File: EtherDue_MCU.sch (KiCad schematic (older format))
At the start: 29 parts, among them IC201 ATSAM3X8E, SW201 ERASE, SW202 RESET, U202 FDN340P, U203 LMV358IDGKR, X201 KX-7 12MHz 20pF, X202 32.768kHz

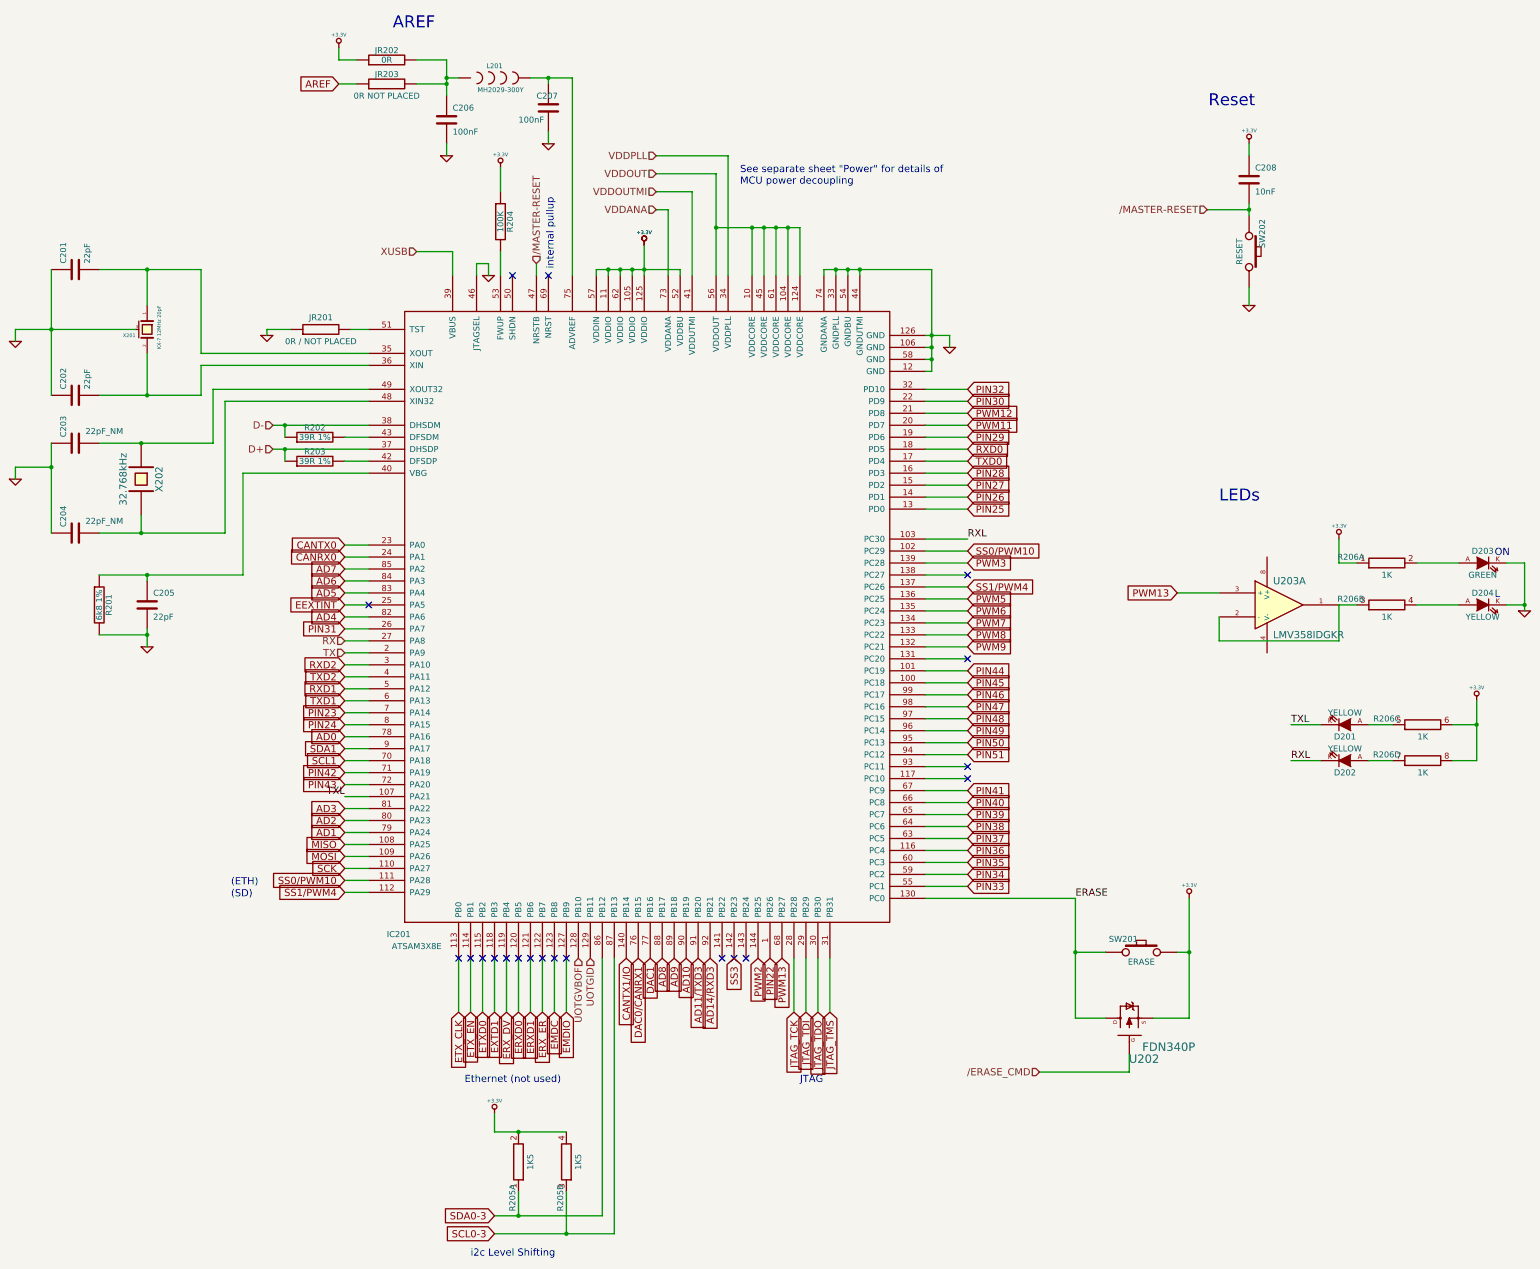
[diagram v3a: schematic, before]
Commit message: Footprints checked, components imported to board but most not placed
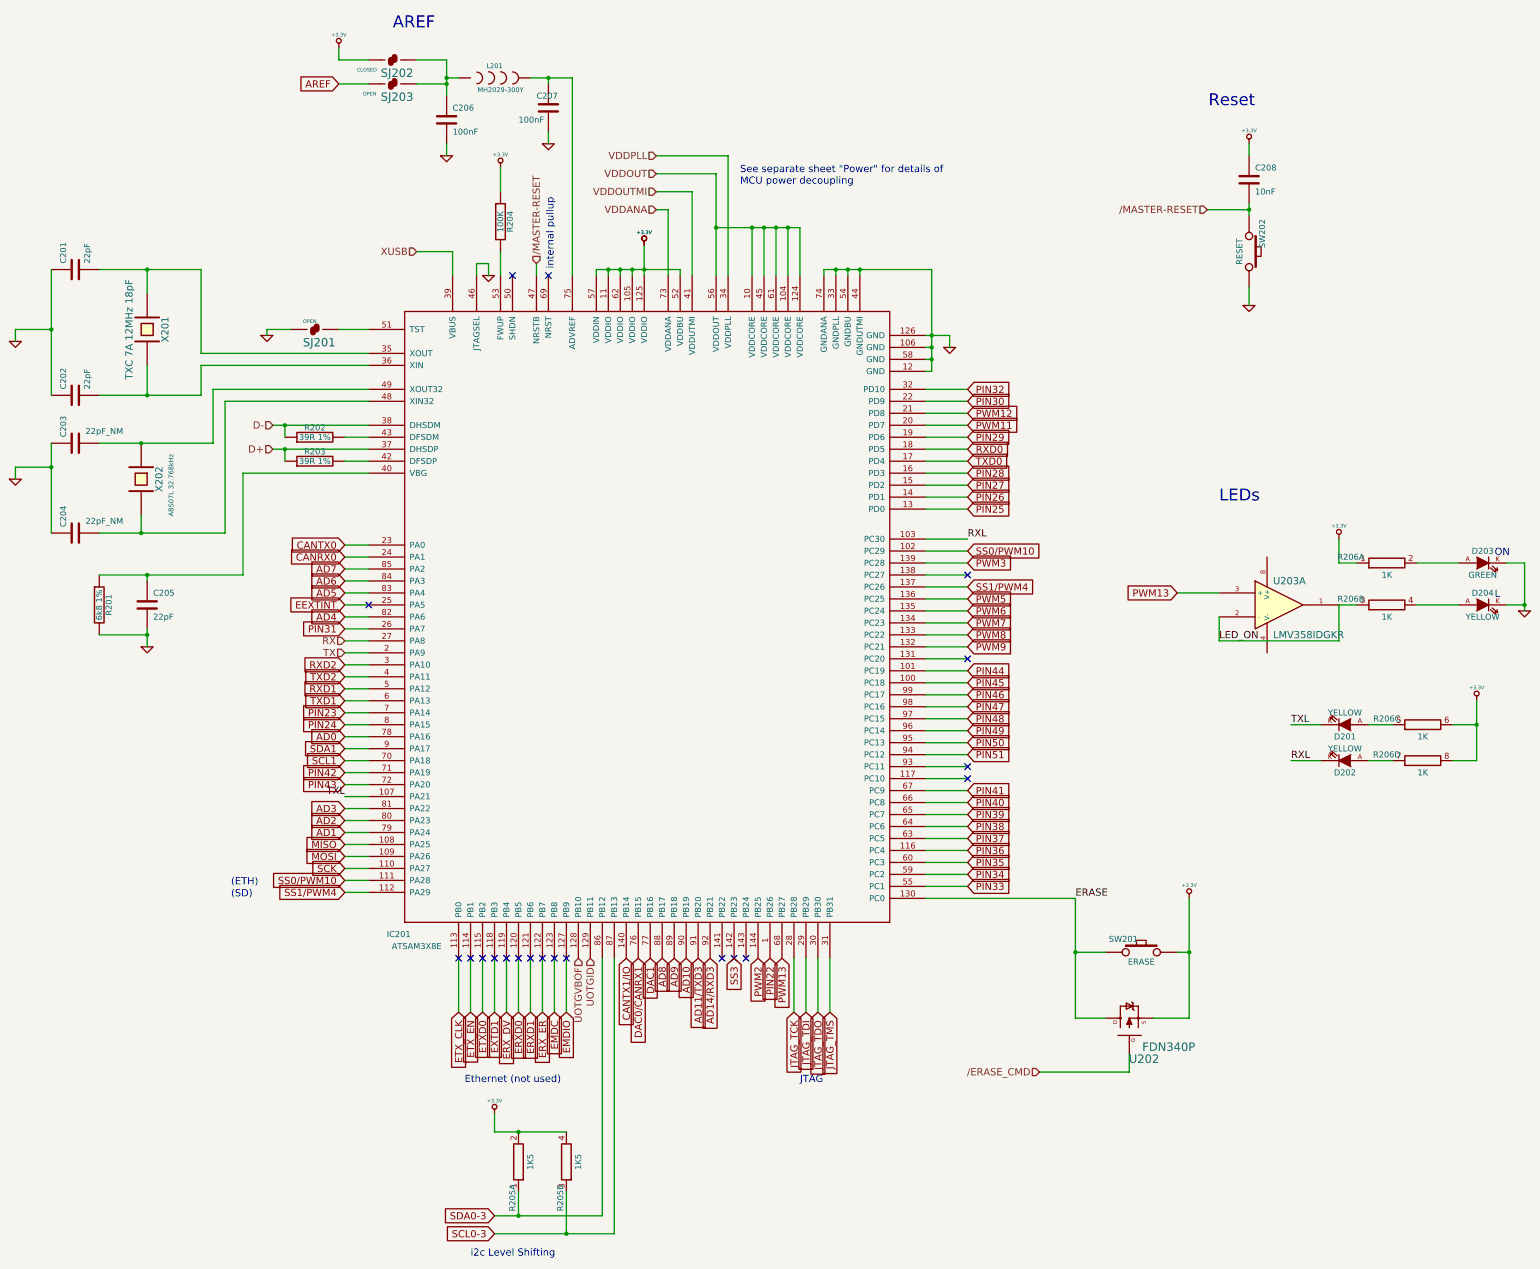
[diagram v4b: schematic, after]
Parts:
- removed JR201: 0R / NOT PLACED, symbol R
- removed JR202: 0R, symbol R
- removed JR203: 0R NOT PLACED, symbol R
- removed X201: KX-7 12MHz 20pF, ~, symbol CRYSTAL_SMD
- added SJ201, SJ203: OPEN, ~, symbol SJ
- added SJ202: CLOSED, ~, symbol SJ
- added X201: TXC 7A 12MHz 18pF, ~, symbol CRYSTAL
- X202: value 32.768kHz -> ABS07L 32.768kHz
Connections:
- net +3.3V: now also SJ202.1
- net AREF: now also SJ203.1
- net GND: now also SJ201.1
- net at C201.2, IC201.35 (XOUT): now also X201.1
- net at C202.2, IC201.36 (XIN): now also X201.2
- net at IC201.51 (TST): now also SJ201.2
- net at C206.1, L201.1: now also SJ202.2, SJ203.2
- net LED_ON: now reaches R206.3 (7), U203.1, U203.2 (-)
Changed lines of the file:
@@
-EESchema Schematic File Version 2  date Tue 04 Jun 2013 15:53:49 EST
+EESchema Schematic File Version 2  date Thu 06 Jun 2013 09:35:07 EST
 LIBS:freetronics_kicad_sch_lib
 LIBS:power
@@
 Sheet 2 6
 Title ""
-Date "4 jun 2013"
+Date "5 jun 2013"
 Rev ""
 Comp ""
@@
 	7700 10750 6700 10750
 Wire Wire Line
-	5400 1150 5550 1150
+	5400 1150 5650 1150
 Connection ~ 6300 1100
 Wire Wire Line
@@
 	4250 2700 4250 3400
 Wire Wire Line
-	5500 3200 5650 3200
+	5400 3200 5650 3200
 Wire Wire Line
 	4800 3250 4800 3200
@@
 	5400 850  5400 950
 Wire Wire Line
-	5400 950  5550 950
+	5400 950  5650 950
 Wire Wire Line
 	7150 1550 7150 1650
@@
 F 3 "" H 6900 10150 60  0001 C CNN
 	1    6900 10150
-	0    -1   -1   0
-$EndComp
-$Comp
-L R JR201
-U 1 1 5163BF82
-P 5250 3200
-F 0 "JR201" V 5350 3200 50  0000 C CNN
-F 1 "0R / NOT PLACED" V 5150 3200 50  0000 C CNN
-F 2 "" H 5250 3200 60  0001 C CNN
-F 3 "" H 5250 3200 60  0001 C CNN
-	1    5250 3200
-	0    -1   -1   0
-$EndComp
-$Comp
-L R JR203
-U 1 1 5163BF2B
-P 5800 1150
-F 0 "JR203" V 5880 1150 50  0000 C CNN
-F 1 "0R NOT PLACED" V 5700 1150 50  0000 C CNN
-F 2 "" H 5800 1150 60  0001 C CNN
-F 3 "" H 5800 1150 60  0001 C CNN
-	1    5800 1150
 	0    -1   -1   0
 $EndComp
@@
 P 3750 4450
 F 0 "X202" H 3750 4600 60  0000 C CNN
-F 1 "32.768kHz" H 3750 4300 60  0000 C CNN
+F 1 "ABS07L 32.768kHz" H 3800 4700 40  0000 C CNN
 F 2 "" H 3750 4450 60  0001 C CNN
 F 3 "" H 3750 4450 60  0001 C CNN
@@
 $EndComp
 $Comp
-L R JR202
-U 1 1 515BA19D
-P 5800 950
-F 0 "JR202" V 5880 950 50  0000 C CNN
-F 1 "0R" V 5800 950 50  0000 C CNN
-F 2 "" H 5800 950 60  0001 C CNN
-F 3 "" H 5800 950 60  0001 C CNN
-	1    5800 950
-	0    -1   -1   0
-$EndComp
-$Comp
 L C C206
 U 1 1 515B9982
@@
 	1    0    0    -1
 $EndComp
-$Comp
-L CRYSTAL_SMD X201
-U 1 1 516FA5C5
+Connection ~ 3800 2700
+Connection ~ 3800 3750
+Wire Wire Line
+	2700 3200 2700 3300
+$Comp
+L CRYSTAL X201
+U 1 1 51AEE4EC
 P 3800 3200
-F 0 "X201" V 3850 3050 30  0000 C CNN
-F 1 "KX-7 12MHz  20pF" H 3600 3300 30  0000 L CNN
+F 0 "X201" H 3800 3350 60  0000 C CNN
+F 1 "TXC 7A 12MHz 18pF" H 3800 3050 60  0000 C CNN
 F 2 "~" H 3800 3200 60  0000 C CNN
 F 3 "~" H 3800 3200 60  0000 C CNN
@@
 $EndComp
 Wire Wire Line
-	2700 3200 3700 3200
-Wire Wire Line
-	3800 3000 3800 2700
-Connection ~ 3800 2700
-Wire Wire Line
-	3800 3400 3800 3750
-Connection ~ 3800 3750
-Wire Wire Line
-	2700 3200 2700 3300
+	2700 3200 3000 3200
+Wire Wire Line
+	3800 2900 3800 2700
+Wire Wire Line
+	3800 3500 3800 3750
+Text Label 12750 5800 0    60   ~ 0
+LED_ON
+$Comp
+L SJ SJ202
+U 1 1 51AFF252
+P 5850 950
+F 0 "SJ202" H 5750 800 70  0000 L BNN
+F 1 "CLOSED" H 5550 850 30  0000 L BNN
+F 2 "~" H 5850 950 60  0000 C CNN
+F 3 "~" H 5850 950 60  0000 C CNN
+	1    5850 950
+	1    0    0    -1
+$EndComp
+$Comp
+L SJ SJ203
+U 1 1 51AFF382
+P 5850 1150
+F 0 "SJ203" H 5750 1000 70  0000 L BNN
+F 1 "OPEN" H 5600 1050 30  0000 L BNN
+F 2 "~" H 5850 1150 60  0000 C CNN
+F 3 "~" H 5850 1150 60  0000 C CNN
+	1    5850 1150
+	1    0    0    -1
+$EndComp
+$Comp
+L SJ SJ201
+U 1 1 51B01054
+P 5200 3200
+F 0 "SJ201" H 5100 3050 70  0000 L BNN
+F 1 "OPEN" H 5100 3250 30  0000 L BNN
+F 2 "~" H 5200 3200 60  0000 C CNN
+F 3 "~" H 5200 3200 60  0000 C CNN
+	1    5200 3200
+	1    0    0    -1
+$EndComp
 $EndSCHEMATC

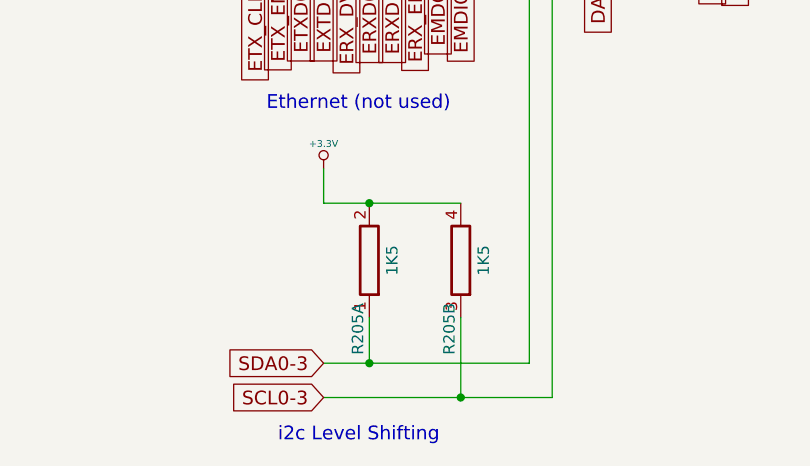
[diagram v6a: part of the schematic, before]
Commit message: All modules placed roughly on PCB
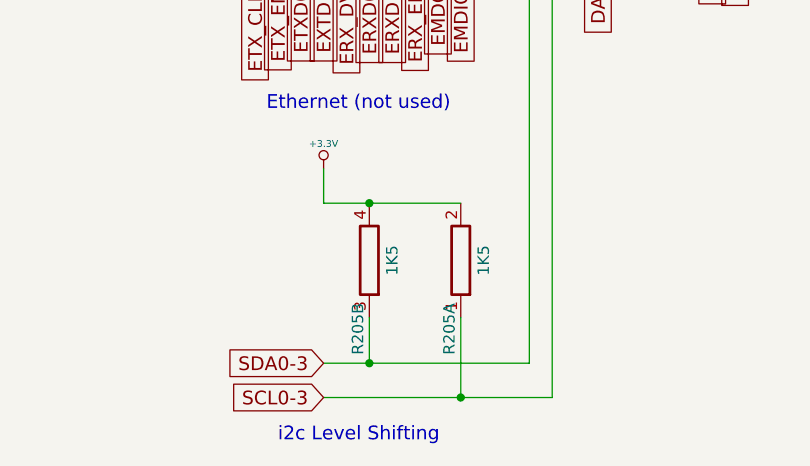
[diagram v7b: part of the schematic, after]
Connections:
- net +3.3V: now also R205.2 (8), R205.4 (8); no longer R205.2 (8), R205.4 (8)
- net SCL0-3: now also R205.1 (7); no longer R205.3 (7)
- net SDA0-3: now also R205.3 (7); no longer R205.1 (7)
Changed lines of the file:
@@
-EESchema Schematic File Version 2  date Thu 06 Jun 2013 10:26:06 EST
+EESchema Schematic File Version 2  date Thu 06 Jun 2013 15:43:54 EST
 LIBS:freetronics_kicad_sch_lib
 LIBS:power
@@
 $Comp
 L RES_PACK4_IND R205
-U 2 1 5163C001
+U 1 1 5163C001
 P 7300 10150
 F 0 "R205" H 7000 10200 50  0000 C CNN
@@
 F 2 "" H 7300 10150 60  0001 C CNN
 F 3 "" H 7300 10150 60  0001 C CNN
-	2    7300 10150
+	1    7300 10150
 	0    -1   -1   0
 $EndComp
 $Comp
 L RES_PACK4_IND R205
-U 1 1 5163BFF9
+U 2 1 5163BFF9
 P 6900 10150
 F 0 "R205" H 6600 10200 50  0000 C CNN
@@
 F 2 "" H 6900 10150 60  0001 C CNN
 F 3 "" H 6900 10150 60  0001 C CNN
-	1    6900 10150
+	2    6900 10150
 	0    -1   -1   0
 $EndComp

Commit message: Tweak schematics, netlist
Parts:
- removed R205: 1K5, symbol RES_PACK4_IND
- added R205, R207: 1K5, ~, symbol R
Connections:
- net +3.3V: now also R205.1, R207.1
- net SCL0-3: now also R207.2
- net SDA0-3: now also R205.2
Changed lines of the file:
@@
-EESchema Schematic File Version 2  date Thu 06 Jun 2013 15:43:54 EST
+EESchema Schematic File Version 2  date Thu 06 Jun 2013 17:31:40 EST
 LIBS:freetronics_kicad_sch_lib
 LIBS:power
@@
 	1    6700 9750
 	1    0    0    -1
-$EndComp
-$Comp
-L RES_PACK4_IND R205
-U 1 1 5163C001
-P 7300 10150
-F 0 "R205" H 7000 10200 50  0000 C CNN
-F 1 "1K5" H 7300 10050 50  0000 C CNN
-F 2 "" H 7300 10150 60  0001 C CNN
-F 3 "" H 7300 10150 60  0001 C CNN
-	1    7300 10150
-	0    -1   -1   0
-$EndComp
-$Comp
-L RES_PACK4_IND R205
-U 2 1 5163BFF9
-P 6900 10150
-F 0 "R205" H 6600 10200 50  0000 C CNN
-F 1 "1K5" H 6900 10050 50  0000 C CNN
-F 2 "" H 6900 10150 60  0001 C CNN
-F 3 "" H 6900 10150 60  0001 C CNN
-	2    6900 10150
-	0    -1   -1   0
 $EndComp
 NoConn ~ 8700 8450
@@
 	1    0    0    -1
 $EndComp
+$Comp
+L R R205
+U 1 1 51B04B7A
+P 6900 10150
+F 0 "R205" V 6980 10150 40  0000 C CNN
+F 1 "1K5" V 6907 10151 40  0000 C CNN
+F 2 "~" V 6830 10150 30  0000 C CNN
+F 3 "~" H 6900 10150 30  0000 C CNN
+	1    6900 10150
+	1    0    0    -1
+$EndComp
+$Comp
+L R R207
+U 1 1 51B04B8E
+P 7300 10150
+F 0 "R207" V 7380 10150 40  0000 C CNN
+F 1 "1K5" V 7307 10151 40  0000 C CNN
+F 2 "~" V 7230 10150 30  0000 C CNN
+F 3 "~" H 7300 10150 30  0000 C CNN
+	1    7300 10150
+	1    0    0    -1
+$EndComp
